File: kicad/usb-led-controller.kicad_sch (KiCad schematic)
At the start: 38 parts, among them J1 SWD, J2 PWR, J3 USB, J4 PWM_0, J5 PWM_1, J6 WS2812_0, J7 WS2812_1, Q1 NVS4409N, Q2 NVS4409N, Q3 NVS4409N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

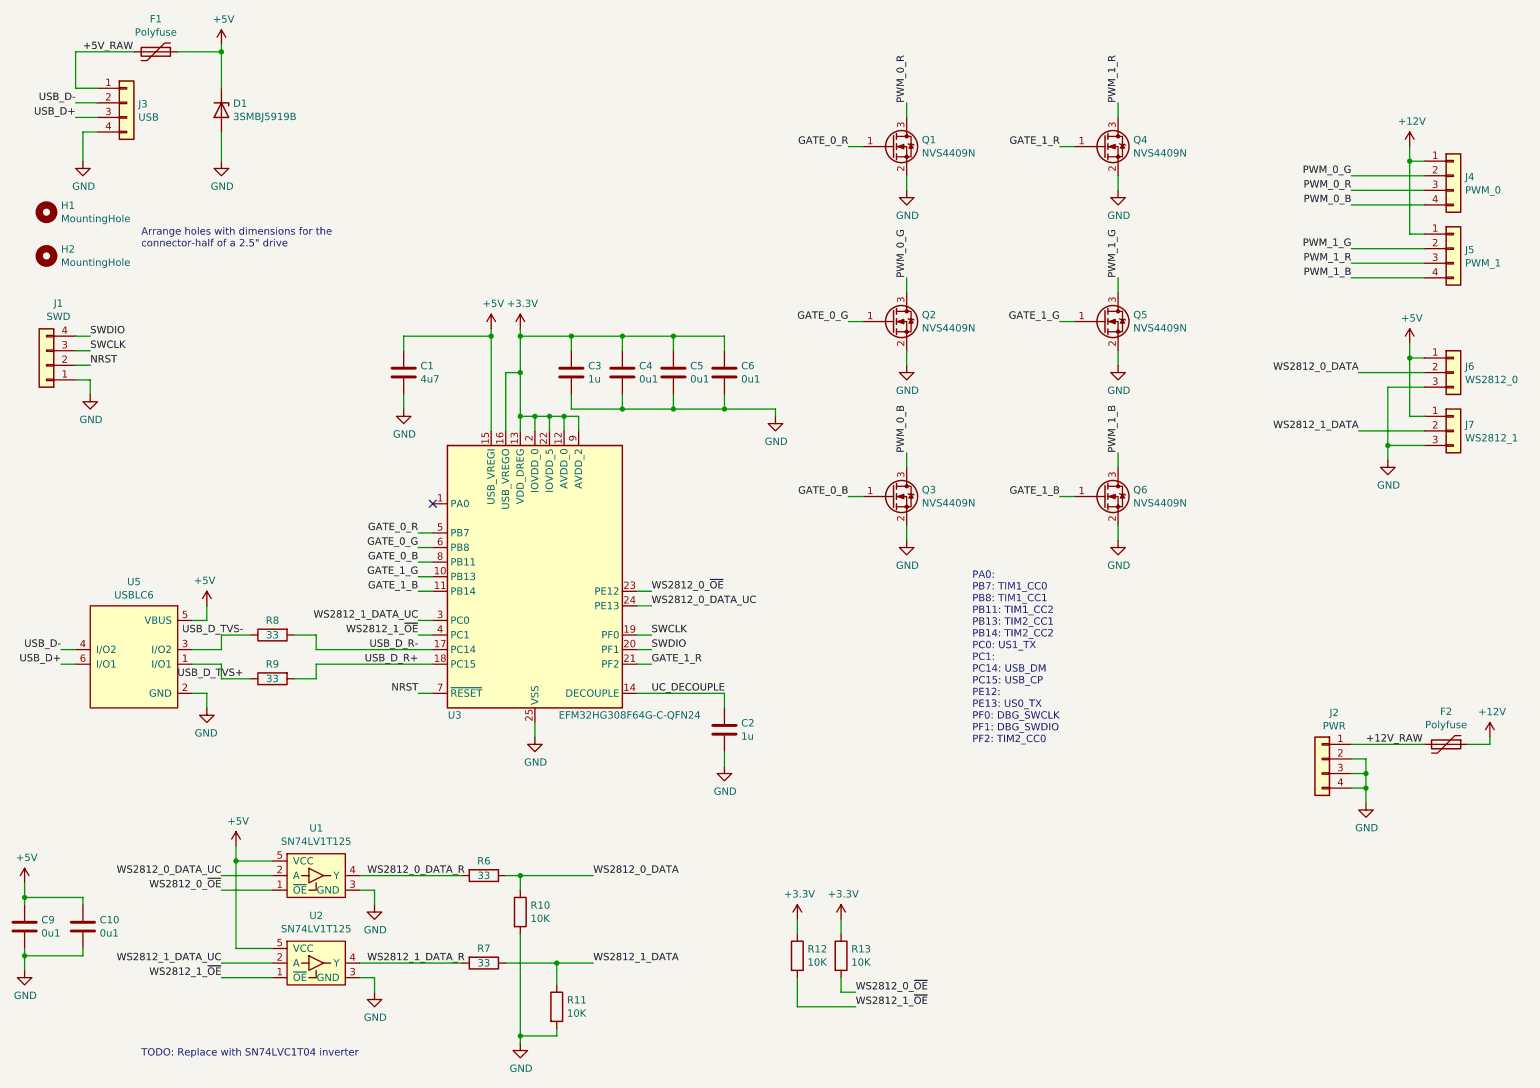
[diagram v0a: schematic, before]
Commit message: Changing microcontroller to ATSAMD21E15B
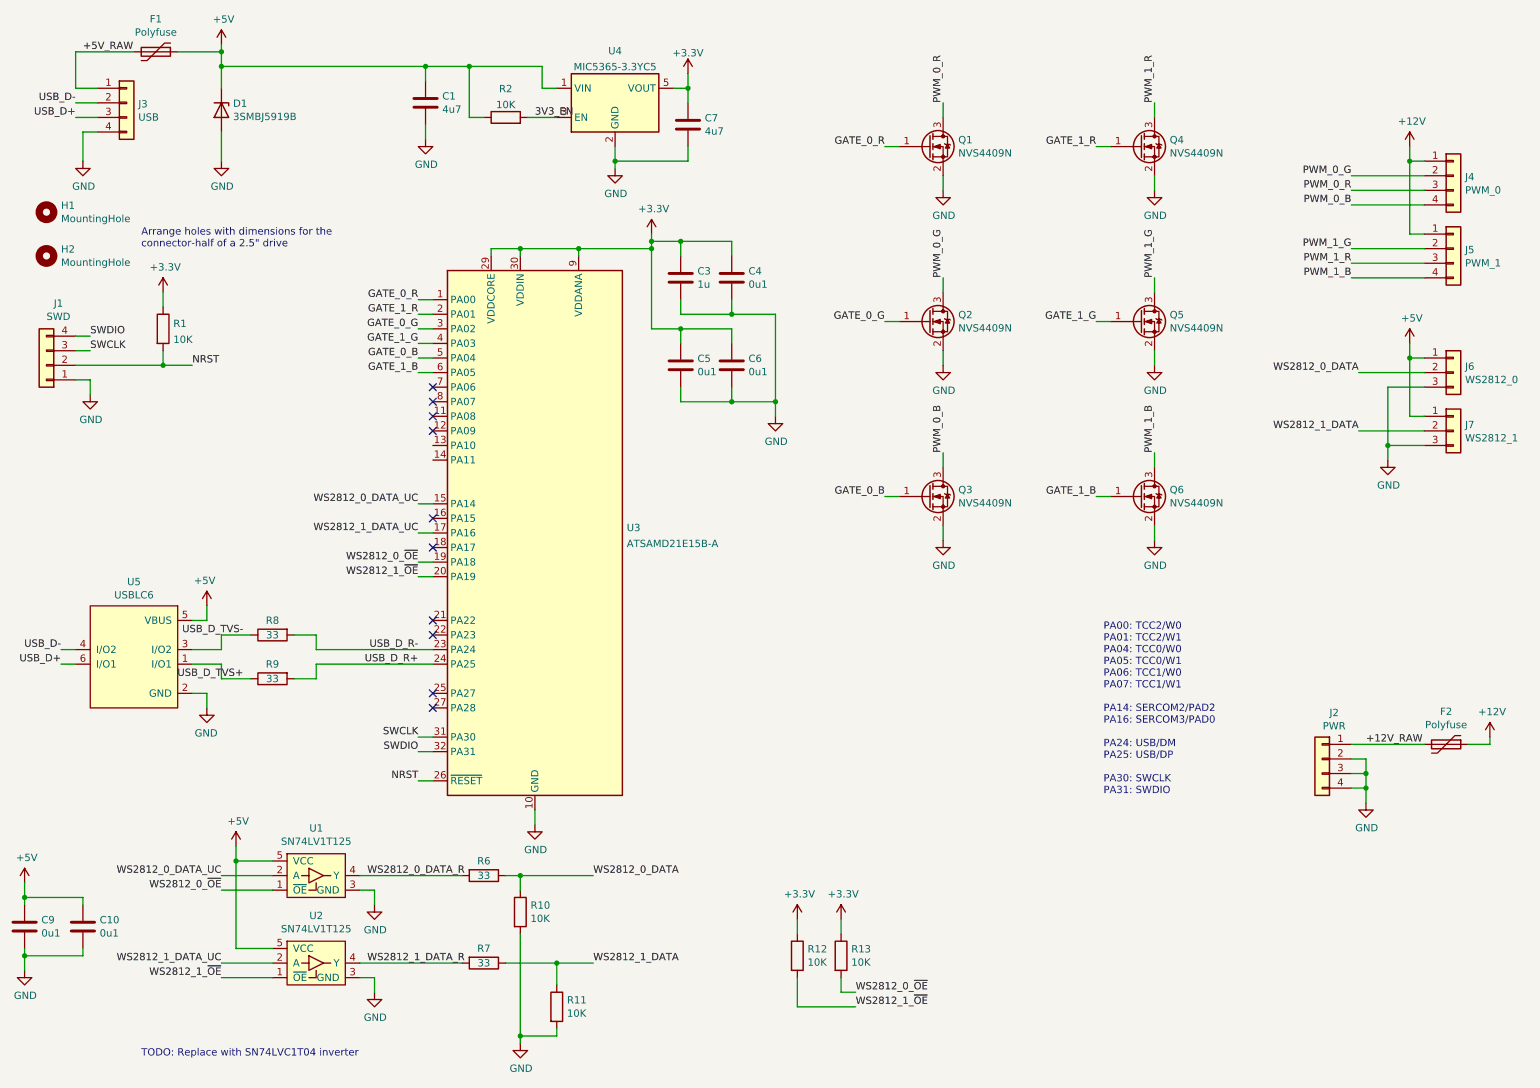
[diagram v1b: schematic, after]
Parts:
- removed C2: 1u, Capacitor_SMD:C_0603_1608Metric, symbol Device:C
- removed U3: EFM32HG308F64G-C-QFN24, Package_DFN_QFN:QFN-24-1EP_5x5mm_P0.65mm_EP3.6x3.6mm_ThermalVias, symbol MCU_SiliconLabs:EFM32HG308F64G-C-QFN24
- added C7: 4u7, Capacitor_SMD:C_0603_1608Metric, symbol Device:C
- added R1: 10K, Resistor_SMD:R_0402_1005Metric, symbol Device:R
- added R2: 10K, symbol Device:R
- added U3: ATSAMD21E15B-A, Package_QFP:TQFP-32_7x7mm_P0.8mm, symbol MCU_Microchip_SAMD:ATSAMD21E15B-A
- added U4: MIC5365-3.3YC5, Package_TO_SOT_SMD:SOT-353_SC-70-5, symbol Regulator_Linear:MIC5365-3.3YC5
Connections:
- net +3V3: now also C7.1, R1.1, U3.29 (VDDCORE), U3.30 (VDDIN), U3.9 (VDDANA), U4.5 (VOUT)
- net +5V: now also R2.1, U4.1 (VIN)
- net GATE_0_B: now also U3.5 (PA04)
- net GATE_0_G: now also U3.3 (PA02)
- net GATE_0_R: now also U3.1 (PA00)
- net GATE_1_B: now also U3.6 (PA05)
- net GATE_1_G: now also U3.4 (PA03)
- net GATE_1_R: now also U3.2 (PA01)
- net GND: now also C7.2, U3.10 (GND), U3.28 (GND), U4.2 (GND)
- net NRST: now also R1.2, U3.26 (~{RESET})
- net SWCLK: now also U3.31 (PA30)
- net SWDIO: now also U3.32 (PA31)
- net USB_D_R+: now also U3.24 (PA25)
- net USB_D_R-: now also U3.23 (PA24)
- net WS2812_0_DATA_UC: now also U3.15 (PA14)
- net WS2812_0_~{OE}: now also U3.19 (PA18)
- net WS2812_1_DATA_UC: now also U3.17 (PA16)
- net WS2812_1_~{OE}: now also U3.20 (PA19)
- new net 3V3_EN: R2.2, U4.3 (EN)
- no-connect marks 1 -> 10
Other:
- note added: "PA00: TCC2/W0 PA01: TCC2/W1 PA04: TCC0/W0 PA05: TCC0/W1 PA06: TCC1/W0 PA07: TCC1/W1 PA14: SERCOM2/PAD2 PA16: SERCOM3/PAD0 PA24: USB/DM PA25: USB/DP PA30: SWCLK PA31: SWDIO"
- note removed: "PA0: PB7: TIM1_CC0 PB8: TIM1_CC1 PB11: TIM1_CC2 PB13: TIM2_CC1 PB14: TIM2_CC2 PC0: US1_TX PC1: PC14: USB_DM PC15: USB_CP PE12: PE13: US0_TX PF0: DBG_SWCLK PF1: DBG_SWDIO PF2: TIM2_CC0"
- moved on the sheet: C1, C3, C4, C5, C6, Q1, Q2, Q3, Q4, Q5, Q6

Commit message: Changing programmer header to standard ARM Cortex one
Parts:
- removed F2: Polyfuse, Resistor_SMD:R_1812_4532Metric, symbol Device:Polyfuse
- removed J1: SWD, usb-led-controller:JST-SH-4, symbol Connector_Generic:Conn_01x04
- added J1: CORTEX-M JTAG, usb-led-controller:CORTEX-SWD-CONNECTOR, symbol Connector_Generic:Conn_02x05_Odd_Even
- added R14, R4, R5: 10K, Resistor_SMD:R_0402_1005Metric, symbol Device:R
- added R15, R16: 33, Resistor_SMD:R_0402_1005Metric, symbol Device:R
- added R3: 0, Resistor_SMD:R_0402_1005Metric, symbol Device:R
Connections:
- net +3V3: now also R14.1, R3.2, R4.1
- net GND: now also J1.3 (Pin_3), J1.5 (Pin_5), J1.9 (Pin_9), R5.2
- net NRST: now also J1.10 (Pin_10)
- net SWCLK: now also J1.4 (Pin_4), R14.2
- net SWDIO: now also J1.2 (Pin_2), R4.2
- net WS2812_0_DATA_UC: now also R15.1; no longer U3.15 (PA14)
- net WS2812_0_~{OE}: now also U3.20 (PA19); no longer U3.19 (PA18)
- net WS2812_1_DATA_UC: now also R16.1; no longer U3.17 (PA16)
- net WS2812_1_~{OE}: now also U3.19 (PA18); no longer U3.20 (PA19)
- new net 3V3_JTAG: J1.1 (Pin_1), R3.1
- new net SWO: J1.6 (Pin_6), R5.1
- new net WS2812_0_DATA_UC_R: R16.2, U3.17 (PA16)
- new net WS2812_1_DATA_UC_R: R15.2, U3.15 (PA14)
- no-connect marks 10 -> 12
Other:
- moved on the sheet: R1

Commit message: Changing FET selection, fixing stackup, adding CYA resistors
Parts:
- added R17, R18: 33, Resistor_SMD:R_0402_1005Metric, symbol Device:R
- added TP1: SWO, TestPoint:TestPoint_Pad_D1.5mm, symbol Connector:TestPoint
- Q1, Q2, Q3, Q4, Q5, Q6: value NVS4409N -> Si1078X; footprint Package_TO_SOT_SMD:SOT-323_SC-70 -> usb-led-controller:SC-89; symbol Device:Q_NMOS_GSD -> Device:Q_NMOS_DGS; Part Number NVS4409NT1GOSCT-ND -> (none)
- R2: footprint (none) -> Resistor_SMD:R_0402_1005Metric
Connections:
- net GATE_0_B: now also Q3.2 (G), U3.7 (PA06); no longer Q3.1 (G), U3.5 (PA04)
- net GATE_0_G: now also Q2.2 (G), U3.5 (PA04); no longer Q2.1 (G), U3.3 (PA02)
- net GATE_0_R: now also Q1.2 (G); no longer Q1.1 (G)
- net GATE_1_B: now also Q6.2 (G), U3.8 (PA07); no longer Q6.1 (G), U3.6 (PA05)
- net GATE_1_G: now also Q5.2 (G), U3.6 (PA05); no longer Q5.1 (G), U3.4 (PA03)
- net GATE_1_R: now also Q4.2 (G); no longer Q4.1 (G)
- net GND: now also Q1.3 (S), Q2.3 (S), Q3.3 (S), Q4.3 (S), Q5.3 (S), Q6.3 (S); no longer Q1.2 (S), Q2.2 (S), Q3.2 (S), Q4.2 (S), Q5.2 (S), Q6.2 (S)
- net PWM_0_B: now also Q3.1 (D); no longer Q3.3 (D)
- net PWM_0_G: now also Q2.1 (D); no longer Q2.3 (D)
- net PWM_0_R: now also Q1.1 (D); no longer Q1.3 (D)
- net PWM_1_B: now also Q6.1 (D); no longer Q6.3 (D)
- net PWM_1_G: now also Q5.1 (D); no longer Q5.3 (D)
- net PWM_1_R: now also Q4.1 (D); no longer Q4.3 (D)
- net SWDIO: now also R18.1; no longer U3.32 (PA31)
- net SWO: now also R17.1, TP1.1
- net SWO_UC: now reaches U3.11 (PA08)
- net SWO_UC: now also R17.2
- new net SWDIO_UC: R18.2, U3.32 (PA31)
- no-connect marks 12 -> 11
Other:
- note added: "PA00: TCC2/W0 PA01: TCC2/W1 PA04: TCC0/W0 PA05: TCC0/W1 PA06: TCC1/W0 PA07: TCC1/W1 PA09: SERCOM2/PAD1 PA14: SERCOM2/PAD2 PA16: SERCOM3/PAD0 PA24: USB/DM PA25: USB/DP PA30: SWCLK PA31: SWDIO"
- note added: "Substituted for 1SMB5920B-13 6.2V. Apparently SMB-2 zeners are hard to come by these days."
- note removed: "PA00: TCC2/W0 PA01: TCC2/W1 PA04: TCC0/W0 PA05: TCC0/W1 PA06: TCC1/W0 PA07: TCC1/W1 PA14: SERCOM2/PAD2 PA16: SERCOM3/PAD0 PA24: USB/DM PA25: USB/DP PA30: SWCLK PA31: SWDIO"
